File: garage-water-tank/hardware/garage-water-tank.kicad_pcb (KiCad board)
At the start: 2 copper layers, 35.3 x 39.4 mm, 9 parts, among them J1 Conn_01x04, J2 Conn_01x04, SW1 SW_Push, U1 XIAO-ESP32-C6-DIP

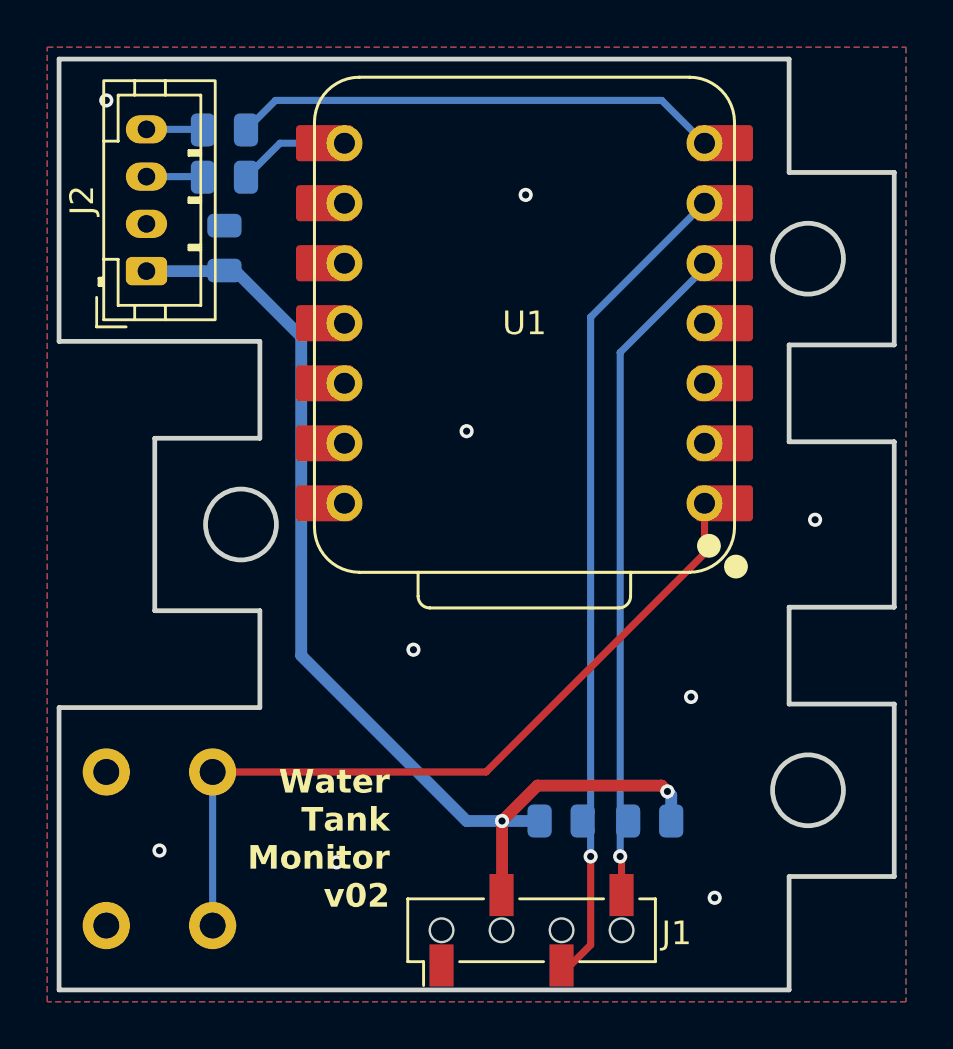
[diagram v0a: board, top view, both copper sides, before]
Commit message: garage-water-tank: socket the XIAO on headers, consolidate to F.Cu
Replaces the directly-mounted XIAO ESP32C6 with the plug-in socket
approach garage-console established: the module has no symbol and no
footprint at all, and its 14 connections are carried by two 1x7 2.54mm
female sockets (HDR1/HDR2) landing on the hybrid footprint's existing
through-holes at the authoritative 15.24mm column spacing. The module
leaves the BOM entirely and is hand-assembled off-board.

With the module gone the space between the header columns frees up, so
R1-R4 and C1 move to F.Cu underneath it, clearing the ~8.5mm the sockets
elevate the module by. That leaves SW1 as the only bottom-side part; it
is hand-soldered, so it is excluded from BOM and position files and
JLCPCB still sees a single-sided assembly. SW1 and J1 are untouched --
identical layer, position, rotation and pad geometry.

Routing was ripped up and redone with Freerouting, then corrected by
hand: VCC to J2 was left unrouted, and its replacement needed moving
clear of the 0.3mm routed-edge rule at the y=68.45 notch.

Also repairs defects the original import carried:
- every symbol recorded (project "Water Tank Monitor") and the PCB
  pointed at a sheetfile that no longer existed; KiCad reads that
  mismatch as unannotated and drops every reference designator
- J1's footprint existed in no library -- it was a custom part from the
  author's personal library, now vendored into garage-water-tank.pretty
- the only absolute path (an unused Button_Switch_SMD fp-lib-table entry
  pointing into /Applications) is gone; everything custom is now
  ${KIPRJMOD}-relative and committed
- PWR_FLAG added for the pre-existing power_pin_not_driven ERC error

ERC is clean. DRC is down to two pre-existing J1 edge-clearance errors
and the intentional HDR1/HDR2 library mismatch that carries the XIAO's
3D model -- note "Update Footprint from Library" on HDR1 would silently
drop it. Board outline and hole positions verified byte-identical to
Wat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
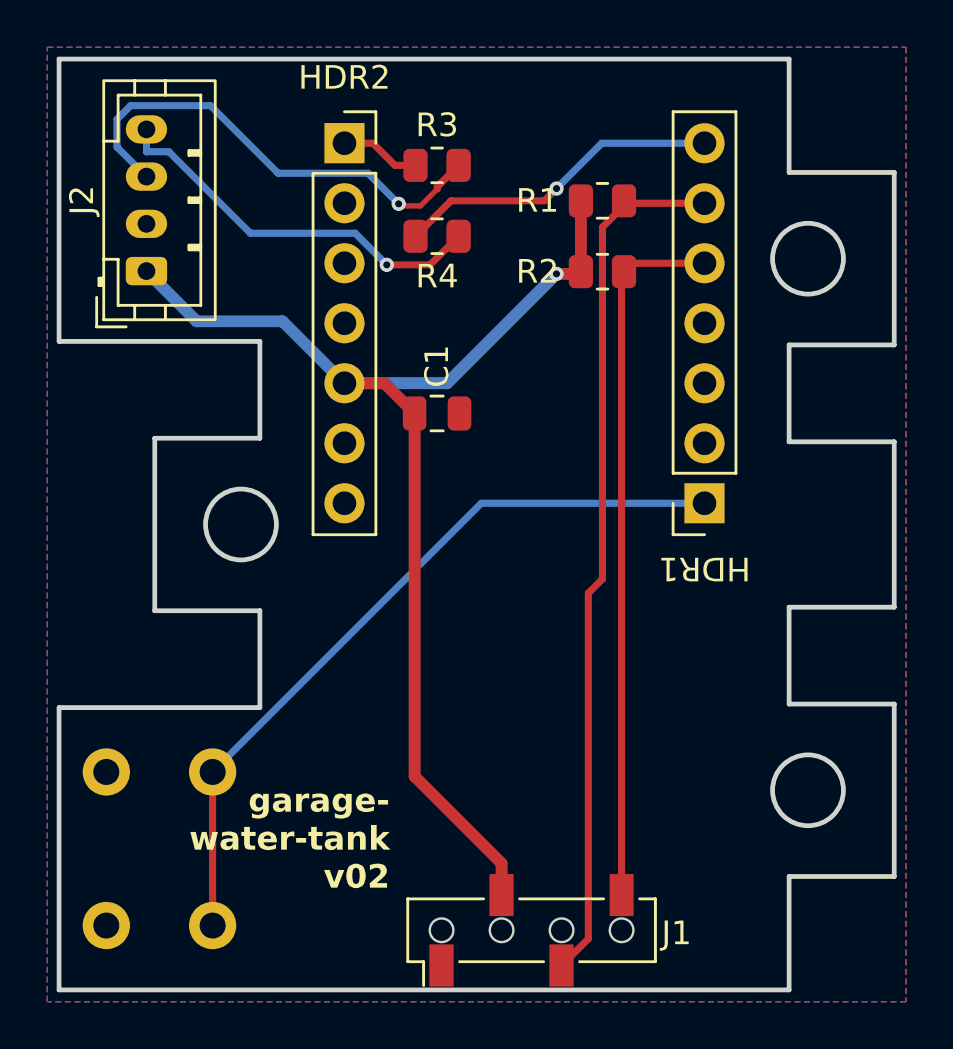
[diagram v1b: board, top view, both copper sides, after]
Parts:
- removed U1: XIAO-ESP32-C6-DIP, Seeed Studio XIAO Series Library:XIAO-ESP32-C6-DIP
- added HDR1: Header_1x7_2.54mm, Connector_PinSocket_2.54mm:PinSocket_1x07_P2.54mm_Vertical, F.Cu at (147.3, 75.3)
- added HDR2: Header_1x7_2.54mm, Connector_PinSocket_2.54mm:PinSocket_1x07_P2.54mm_Vertical, F.Cu at (132.1, 60.1)
- C1, R1, R2, R3, R4: moved to F.Cu
- J1: footprint Connector_PinSocket_2.54mm:PinSocket_1x04_P2.54mm_Vertical_SMD_low_profile_Pin1Left -> garage-water-tank:PinSocket_1x04_P2.54mm_Vertical_SMD_low_profile_Pin1Left
- moved R1 26.3 mm to (143.0, 62.5)
- moved R2 23.3 mm to (143.0, 65.5), turned to 0 degrees
- moved C1 11.4 mm to (136.0, 71.5), turned to 0 degrees
- moved R4 10.1 mm to (136.0, 64.0), turned to 0 degrees
- moved R3 9.01 mm to (136.0, 61.0), turned to 0 degrees
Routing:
- net Net-(J2-Pin_3): track 2.40 -> 20.2 mm, vias 0 -> 1
- net Net-(J2-Pin_4): track 2.40 -> 16.6 mm, vias 0 -> 1
- net TX: track 20.7 -> 13.9 mm, vias 0 -> 1
- net VCC: track 48.1 -> 50.7 mm, vias 2 -> 1
- net SCL: track 35.3 -> 36.8 mm, vias 1 -> 0
- net RX: track 4.76 -> 3.40 mm
- net SDA: track 28.7 -> 30.0 mm, vias 1 -> 0
- net ACT: track 33.3 -> 32.0 mm
- net GND: vias 9 -> 0
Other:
- board text added: "garage- water-tank v02"
- board text removed: "Water Tank Monitor v02"

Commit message: garage-water-tank: regenerate fab files, add CPL corrections, fix R2's library
Generates the upload-ready JLCPCB package (gerbers, drill, BOM, CPL) for
the socketed layout, tracked the way garage-console tracks its own.

Adds jlcpcb-cpl-corrections.json. HDR1/HDR2 need the same pin-1-anchor
compensation garage-console documented: Konnect writes the footprint
anchor into CPL Mid X/Mid Y rather than the component midpoint
(Konnect #667), so the 1x7 sockets land 7.62mm out in opposite board-Y
directions. With the offsets applied both headers land on y=-67.6815,
the line they physically share. J2 needs +3.0mm in X for the same
reason (JST PH pads at local x 0/2/4/6). The 90 deg socket rotation is
carried over from garage-console, where this exact footprint was
verified in JLCPCB's placement preview; J1 and J2 rotations are NOT yet
verified and are called out as such in the policy's provenance.

Fixes R2, which pointed at "Resistor_SMD_test:R_0805_2012Metric" -- a
nickname that resolves in no library table and matches no .pretty on
disk. Its geometry is identical to R1/R3/R4's stock
Resistor_SMD:R_0805_2012Metric, and the dangling nickname was splitting
two identical 4k7 0805s across separate BOM lines. Every footprint
nickname on the board now resolves.

SW1 is correctly absent from both BOM and CPL.

Not ready to order: validate_for_manufacturing returns NOT READY on the
two pre-existing J1 copper-edge-clearance errors (its own Edge.Cuts
circles sit 0.1mm from its pads against a 0.5mm rule), and every part
except J2 still lacks an LCSC number.

Co-Authored-By: Claude Opus 5 (1M context) <noreply@anthropic.com>
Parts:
- R2: footprint Resistor_SMD_test:R_0805_2012Metric -> Resistor_SMD:R_0805_2012Metric
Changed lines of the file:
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@@
 		)
 	)
-	(footprint "Resistor_SMD_test:R_0805_2012Metric"
+	(footprint "Resistor_SMD:R_0805_2012Metric"
 		(layer "F.Cu")
 		(at 143 65.5)

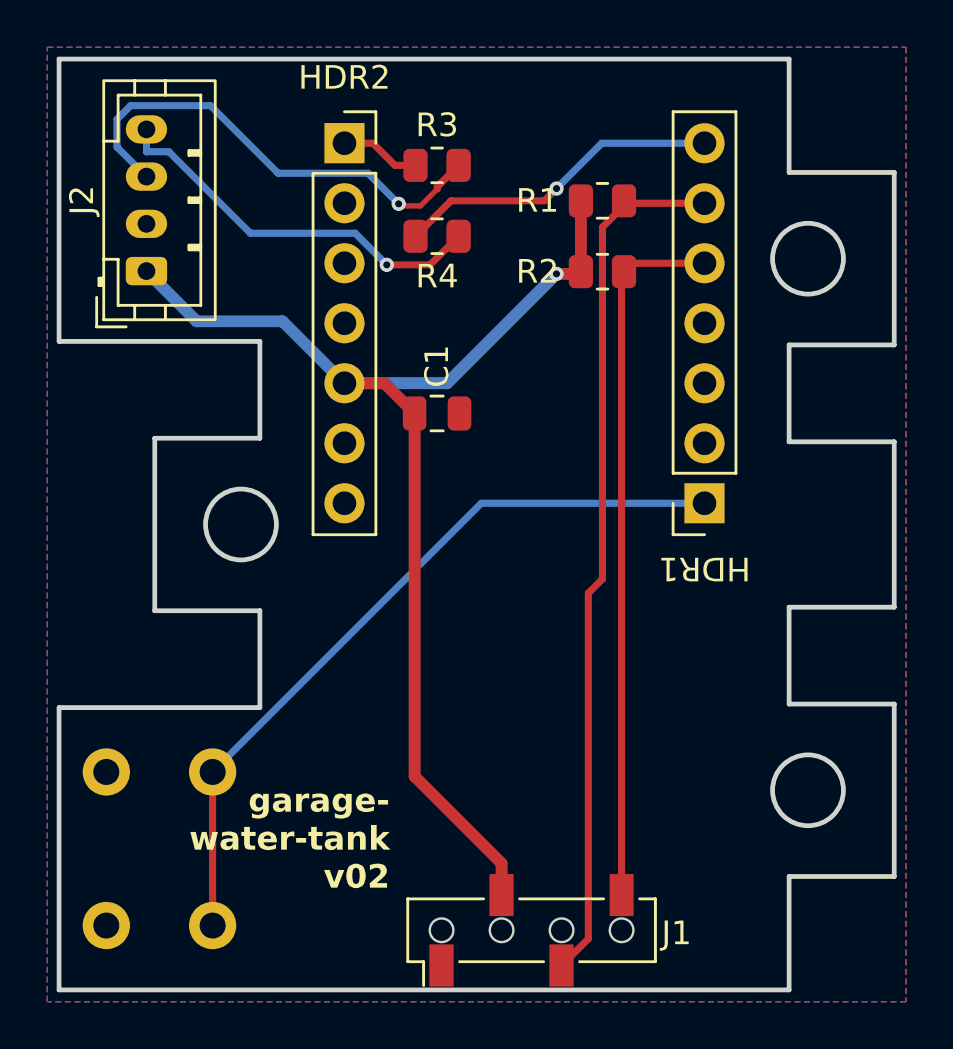
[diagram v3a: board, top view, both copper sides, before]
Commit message: garage-water-tank: hand-tuned routing, restore board metadata, refresh fab files
Manual routing cleanup by the project owner: total track length drops
203.66mm -> 194.67mm and the via count halves from 4 to 2, with VCC and
both J2 signal nets shortened and only +0.2mm added on SCL. C1 moves to
(137.25, 70.25). Still zero unconnected items, and no track introduces a
DRC violation.

That work was saved from a PCB editor session opened before the previous
two commits, which silently rolled back three board-side changes. The
schematic was untouched and stayed correct, so this restores the board
to agree with it:

- R2's footprint had reverted to "Resistor_SMD_test:R_0805_2012Metric",
  the nickname that resolves in no library table
- LCSC fields had been dropped from R1-R4, HDR1, HDR2 and J1
- J2 had reverted to LCSC C144395 / MPN "B4B-XH-A" -- the JST XH at
  2.5mm pitch that cannot fit this board's 2.00mm PH footprint

Schematic parity was reporting 9 issues as a result; it is back to zero.

Fab files regenerated against the new routing. BOM still carries an LCSC
number on every line, and the CPL picks up C1's new position while both
headers stay on the shared y=-67.6815 midpoint line.

Unchanged: the two pre-existing J1 copper-edge-clearance errors, which
still hold back a READY verdict.

Co-Authored-By: Claude Opus 5 (1M context) <noreply@anthropic.com>
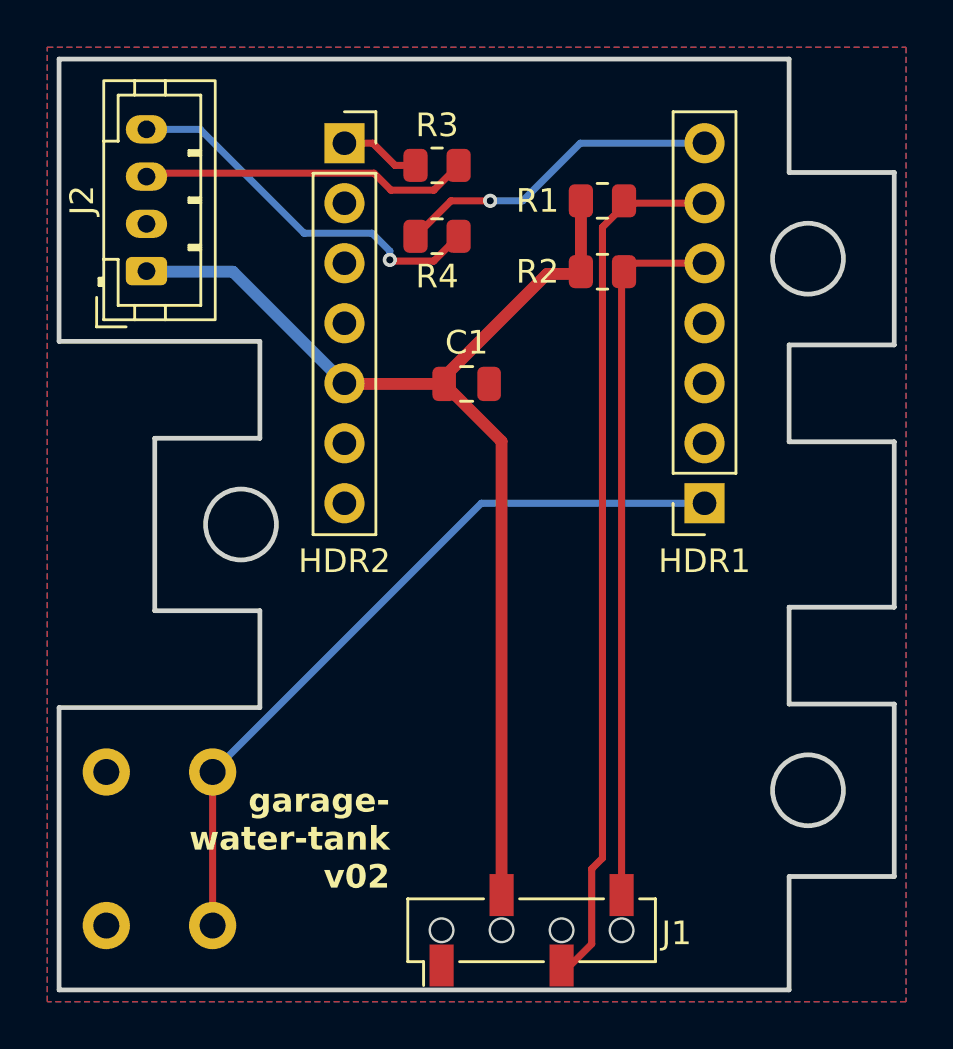
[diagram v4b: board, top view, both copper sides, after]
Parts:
- moved C1 1.77 mm to (137.2, 70.2)
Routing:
- net Net-(J2-Pin_3): track 20.2 -> 14.0 mm, vias 1 -> 0
- net VCC: track 50.7 -> 48.2 mm, vias 1 -> 0
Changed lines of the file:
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@@
 		(at 132.08 60.0615)
 		(property "Reference" "HDR2"
-			(at 0 -2.77 0)
+			(at 0 17.6885 0)
 			(unlocked yes)
 			(layer "F.SilkS")
@@
 		(at 147.32 75.3015 180)
 		(property "Reference" "HDR1"
-			(at 0 -2.77 180)
+			(at 0 -2.4485 0)
 			(unlocked yes)
 			(layer "F.SilkS")
@@
 	(footprint "Capacitor_SMD:C_0805_2012Metric"
 		(layer "F.Cu")
-		(at 136 71.5)
+		(at 137.25 70.25)
 		(descr "Capacitor SMD 0805 (2012 Metric), square (rectangular) end terminal, IPC-7351 nominal, (Body size source: IPC-SM-782 page 76, https://www.pcb-3d.com/wordpress/wp-content/uploads/ipc-sm-782a_amendment_1_and_2.pdf, https://docs.google.com/spreadsheets/d/1BsfQQcO9C6DZCsRaXUlFlo91Tg2WpOkGARC1WS5S8t0/edit?usp=sharing)")
 		(tags "capacitor")
 		(property "Reference" "C1"
-			(at 0 -2 90)
+			(at 0 -1.75 180)
 			(layer "F.SilkS")
 			(effects
@@
 	)
 	(segment
-		(start 135.05 71.5)
-		(end 135.05 86.8633)
+		(start 136.3 70.25)
+		(end 132.1085 70.25)
 		(width 0.5)
 		(layer "F.Cu")
@@
 	)
 	(segment
-		(start 132.08 70.2215)
-		(end 133.7715 70.2215)
+		(start 140.6568 65.5932)
+		(end 141.9943 65.5932)
 		(width 0.5)
 		(layer "F.Cu")
@@
 	)
 	(segment
-		(start 133.7715 70.2215)
-		(end 135.05 71.5)
+		(start 136.3 69.95)
+		(end 136.3 70.25)
 		(width 0.5)
 		(layer "F.Cu")
@@
 	)
 	(segment
-		(start 138.73 91.885)
-		(end 138.73 90.5433)
+		(start 141.9943 65.5932)
+		(end 142.0875 65.5)
 		(width 0.5)
 		(layer "F.Cu")
@@
 	)
 	(segment
-		(start 141.0558 65.5932)
-		(end 141.9943 65.5932)
+		(start 132.1085 70.25)
+		(end 132.08 70.2215)
 		(width 0.5)
 		(layer "F.Cu")
@@
 	)
 	(segment
-		(start 135.05 86.8633)
-		(end 138.73 90.5433)
+		(start 138.73 91.885)
+		(end 138.73 72.68)
 		(width 0.5)
 		(layer "F.Cu")
@@
 	)
 	(segment
-		(start 141.9943 65.5932)
-		(end 142.0875 65.5)
+		(start 140.6568 65.5932)
+		(end 136.3 69.95)
 		(width 0.5)
 		(layer "F.Cu")
@@
 	)
 	(segment
-		(start 142.0875 62.5)
-		(end 142.0875 65.5)
+		(start 138.73 72.68)
+		(end 136.3 70.25)
 		(width 0.5)
 		(layer "F.Cu")
 		(net "VCC")
 	)
-	(via
-		(at 141.0558 65.5932)
-		(size 0.6)
-		(drill 0.3)
-		(layers "F.Cu" "B.Cu")
-		(net "VCC")
-	)
 	(segment
-		(start 141.0558 65.5932)
-		(end 136.4275 70.2215)
-		(width 0.5)
-		(layer "B.Cu")
-		(net "VCC")
-	)
-	(segment
-		(start 129.46 67.6)
-		(end 132.08 70.222)
+		(start 142.0875 62.5)
+		(end 142.0875 65.5)
 		(width 0.5)
-		(layer "B.Cu")
+		(layer "F.Cu")
 		(net "VCC")
 	)
 	(segment
-		(start 136.4275 70.2215)
-		(end 132.08 70.2215)
+		(start 123.7 65.475)
+		(end 123.725 65.5)
 		(width 0.5)
 		(layer "B.Cu")
@@
 	)
 	(segment
-		(start 123.7 65.475)
-		(end 125.825 67.6)
+		(start 127.358 65.5)
+		(end 132.08 70.222)
 		(width 0.5)
 		(layer "B.Cu")
@@
 	)
 	(segment
-		(start 125.825 67.6)
-		(end 129.46 67.6)
+		(start 123.725 65.5)
+		(end 127.358 65.5)
 		(width 0.5)
 		(layer "B.Cu")
@@
 	)
 	(segment
-		(start 142.403 93.732)
-		(end 142.403 79.1057)
+		(start 143 90.3225)
+		(end 143 63.6155)
 		(width 0.3)
 		(layer "F.Cu")
@@
 	)
 	(segment
-		(start 143 63.6155)
-		(end 144.014 62.6015)
+		(start 141.27 94.865)
+		(end 141.635 94.865)
 		(width 0.3)
 		(layer "F.Cu")
@@
 	)
 	(segment
-		(start 143 78.5087)
-		(end 143 63.6155)
+		(start 142.546396 90.776104)
+		(end 143 90.3225)
 		(width 0.3)
 		(layer "F.Cu")
@@
 	)
 	(segment
-		(start 141.27 94.865)
-		(end 142.403 93.732)
+		(start 141.635 94.865)
+		(end 142.546396 93.953604)
 		(width 0.3)
 		(layer "F.Cu")
@@
 	)
 	(segment
-		(start 142.403 79.1057)
-		(end 143 78.5087)
+		(start 142.546396 93.953604)
+		(end 142.546396 90.776104)
 		(width 0.3)
 		(layer "F.Cu")
@@
 	)
 	(segment
-		(start 136.5875 62.5)
-		(end 135.0875 64)
+		(start 143 63.6155)
+		(end 144.014 62.6015)
 		(width 0.3)
 		(layer "F.Cu")
-		(net "TX")
+		(net "SCL")
 	)
 	(segment
-		(start 141.0558 61.9808)
-		(end 140.5366 62.5)
+		(start 138.25 62.5)
+		(end 136.5875 62.5)
 		(width 0.3)
 		(layer "F.Cu")
@@
 	)
 	(segment
-		(start 140.5366 62.5)
-		(end 136.5875 62.5)
+		(start 136.5875 62.5)
+		(end 135.0875 64)
 		(width 0.3)
 		(layer "F.Cu")
@@
 	)
 	(via
-		(at 141.0558 61.9808)
+		(at 138.25 62.5)
 		(size 0.6)
 		(drill 0.3)
@@
 	)
 	(segment
-		(start 141.0558 61.9808)
-		(end 142.9751 60.0615)
+		(start 138.25 62.5)
+		(end 139.625 62.5)
 		(width 0.3)
 		(layer "B.Cu")
@@
 	)
 	(segment
-		(start 142.9751 60.0615)
-		(end 147.32 60.0615)
+		(start 139.625 62.5)
+		(end 142.0635 60.0615)
 		(width 0.3)
 		(layer "B.Cu")
@@
 	)
 	(segment
-		(start 135.3007 62.7144)
-		(end 136.0106 62.0045)
-		(width 0.225)
-		(layer "F.Cu")
-		(net "Net-(J2-Pin_3)")
-	)
-	(segment
-		(start 134.3748 62.6279)
-		(end 134.4613 62.7144)
+		(start 142.0635 60.0615)
+		(end 147.32 60.0615)
 		(width 0.3)
-		(layer "F.Cu")
-		(net "Net-(J2-Pin_3)")
+		(layer "B.Cu")
+		(net "TX")
 	)
 	(segment
-		(start 136.0106 61.9019)
-		(end 136.9125 61)
+		(start 134.05 62.05)
+		(end 133.330562 61.330562)
 		(width 0.3)
 		(layer "F.Cu")
@@
 	)
 	(segment
-		(start 134.4613 62.7144)
-		(end 135.3007 62.7144)
-		(width 0.225)
-		(layer "F.Cu")
-		(net "Net-(J2-Pin_3)")
-	)
-	(segment
-		(start 136.0106 62.0045)
-		(end 136.0106 61.9019)
+		(start 135.8625 62.05)
+		(end 134.05 62.05)
 		(width 0.3)
 		(layer "F.Cu")
 		(net "Net-(J2-Pin_3)")
 	)
-	(via
-		(at 134.3748 62.6279)
-		(size 0.6)
-		(drill 0.3)
-		(layers "F.Cu" "B.Cu")
-		(net "Net-(J2-Pin_3)")
-	)
-	(segment
-		(start 129.2697 61.3314)
-		(end 133.0783 61.3314)
-		(width 0.3)
-		(layer "B.Cu")
-		(net "Net-(J2-Pin_3)")
-	)
-	(segment
-		(start 122.4541 60.2291)
-		(end 122.4541 59.0442)
-		(width 0.3)
-		(layer "B.Cu")
-		(net "Net-(J2-Pin_3)")
-	)
 	(segment
-		(start 123.0274 58.4709)
-		(end 126.4092 58.4709)
+		(start 136.9125 61)
+		(end 135.8625 62.05)
 		(width 0.3)
-		(layer "B.Cu")
-		(net "Net-(J2-Pin_3)")
-	)
-	(segment
-		(start 133.0783 61.3314)
-		(end 134.3748 62.6279)
-		(width 0.3)
-		(layer "B.Cu")
+		(layer "F.Cu")
 		(net "Net-(J2-Pin_3)")
 	)
 	(segment
-		(start 126.4092 58.4709)
-		(end 129.2697 61.3314)
+		(start 133.330562 61.330562)
+		(end 123.844438 61.330562)
 		(width 0.3)
-		(layer "B.Cu")
+		(layer "F.Cu")
 		(net "Net-(J2-Pin_3)")
 	)
 	(segment
-		(start 123.7 61.475)
-		(end 122.4541 60.2291)
+		(start 123.844438 61.330562)
+		(end 123.7 61.475)
 		(width 0.3)
-		(layer "B.Cu")
+		(layer "F.Cu")
 		(net "Net-(J2-Pin_3)")
 	)
 	(segment
-		(start 122.4541 59.0442)
-		(end 123.0274 58.4709)
+		(start 134.05 65.05)
+		(end 134 65)
 		(width 0.3)
-		(layer "B.Cu")
-		(net "Net-(J2-Pin_3)")
+		(layer "F.Cu")
+		(net "Net-(J2-Pin_4)")
 	)
 	(segment
-		(start 135.7023 65.2102)
-		(end 136.9125 64)
+		(start 135.8625 65.05)
+		(end 134.05 65.05)
 		(width 0.3)
 		(layer "F.Cu")
@@
 	)
 	(segment
-		(start 133.8713 65.2102)
-		(end 135.7023 65.2102)
+		(start 136.9125 64)
+		(end 135.8625 65.05)
 		(width 0.3)
 		(layer "F.Cu")
@@
 	)
 	(via
-		(at 133.8713 65.2102)
+		(at 134 65)
 		(size 0.6)
 		(drill 0.3)
@@
 	)
 	(segment
-		(start 123.7 59.475)
-		(end 123.7 60.4267)
+		(start 134 65)
+		(end 134 64.625)
 		(width 0.3)
 		(layer "B.Cu")
@@
 	)
 	(segment
-		(start 128.0965 63.8715)
-		(end 132.5326 63.8715)
+		(start 130.3715 63.8715)
+		(end 125.975 59.475)
 		(width 0.3)
 		(layer "B.Cu")
@@
 	)
 	(segment
-		(start 132.5326 63.8715)
-		(end 133.8713 65.2102)
+		(start 134 64.625)
+		(end 133.2465 63.8715)
 		(width 0.3)
 		(layer "B.Cu")
@@
 	)
 	(segment
-		(start 123.7 60.4267)
-		(end 124.6517 60.4267)
+		(start 125.975 59.475)
+		(end 123.7 59.475)
 		(width 0.3)
 		(layer "B.Cu")
@@
 	)
 	(segment
-		(start 124.6517 60.4267)
-		(end 128.0965 63.8715)
+		(start 133.2465 63.8715)
+		(end 130.3715 63.8715)
 		(width 0.3)
 		(layer "B.Cu")
